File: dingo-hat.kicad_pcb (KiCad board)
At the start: 4 copper layers, 65 x 56.5 mm, 91 parts, among them J1 LiPo-Power, J10 PJ-037B, J11 Bypass-Power, J12 Chassis-Out, J13 i2c_display, J14 WS2812, J15 MPU-9250, J2 Raspberry_Pi_2_3, J201 Bootstrap, J24 3mm_Mount, J25 3mm_Mount, J26 3mm_Mount, J27 3mm_Mount, J3 ULTRA_0, J4 ULTRA_1, J5 LiPo-Balance, J6 0, J7 1, J8 2, J9 3, U1 MCP3021, U2 PCA9685PW, U201 AP9211, U202 MCP73213T-A6BI_MF, U203 BQ29209DRBR, U301 AOZ6605PI-1

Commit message: Updated footprints
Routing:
- net +5V: track 4.96 -> 176.7 mm, vias 16 -> 5
- net +3V3: track 106.7 -> 93.5 mm
- net Net-(F1-Pad2): track 5.06 -> 0.00 mm
- net /SCL_3.3: track 64.5 -> 63.2 mm
- net Net-(J8-Pad3): track 24.9 -> 24.4 mm
- net /SDA_3.3: vias 2 -> 3
- removed copper zone on In2.Cu, net +5V
- removed copper zone on In1.Cu, net GND

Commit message: Changed and re-routed to be 2 layer
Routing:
- net GND: track 46.8 -> 57.2 mm, vias 72 -> 89
- net Net-(FB1-Pad2): track 1.53 -> 6.48 mm
- net Net-(F1-Pad2): track 0.00 -> 4.23 mm
- net /VC0: track 35.0 -> 34.3 mm
- net +5V: track 176.7 -> 176.0 mm
- net /SDA_3.3: track 68.5 -> 69.1 mm, vias 3 -> 2
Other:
- copper layers 4 -> 2

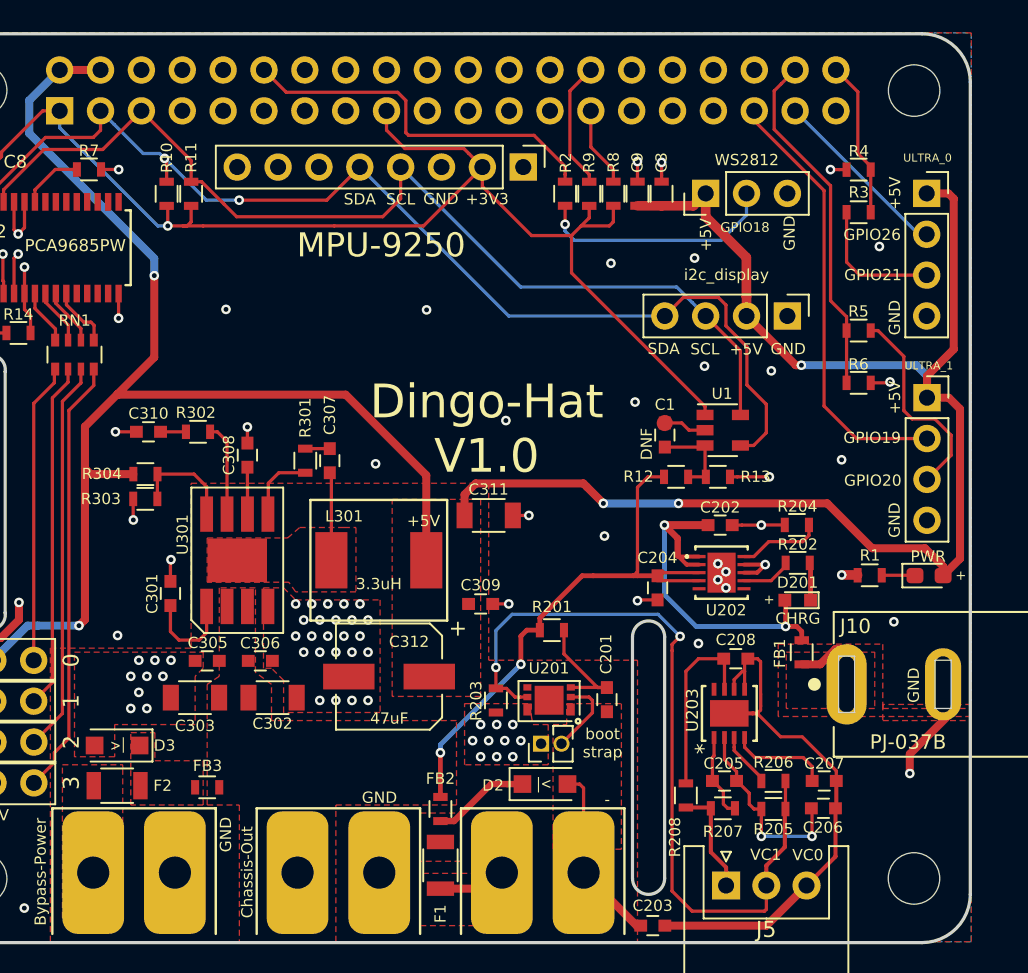
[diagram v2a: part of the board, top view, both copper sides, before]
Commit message: updated footprints to handsolder
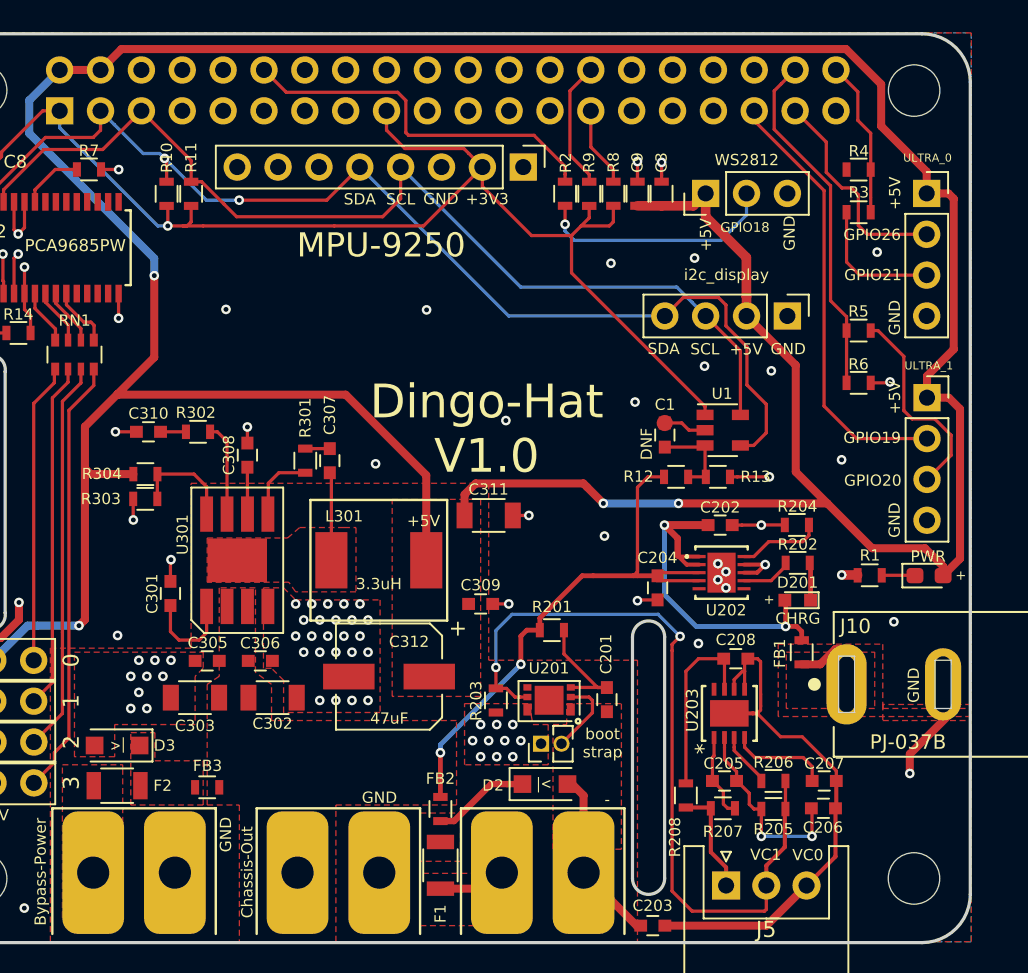
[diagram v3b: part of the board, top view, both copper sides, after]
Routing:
- net +5V: track 176.0 -> 233.6 mm, vias 5 -> 4
- net /GPIO26: track 11.4 -> 13.6 mm
- net GND: track 57.2 -> 56.2 mm, vias 89 -> 88
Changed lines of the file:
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@@
     (thickness 1.6)
     (drawings 94)
-    (tracks 613)
+    (tracks 619)
     (zones 0)
     (modules 91)
@@
   )
   (setup
-    (last_trace_width 0.5)
+    (last_trace_width 0.2032)
     (user_trace_width 0.1524)
     (user_trace_width 0.2032)
@@
   (via (at 144.31 51.444) (size 0.6) (drill 0.3) (layers F.Cu B.Cu) (net 1))
   (segment (start 144.31 52.2408) (end 144.31 51.444) (width 0.2032) (layer F.Cu) (net 1))
-  (segment (start 157.31 51.944) (end 156.8568 51.944) (width 0.2032) (layer F.Cu) (net 1))
-  (via (at 156.31 51.944) (size 0.6) (drill 0.3) (layers F.Cu B.Cu) (net 1))
-  (segment (start 156.8568 51.944) (end 156.31 51.944) (width 0.2032) (layer F.Cu) (net 1))
   (segment (start 148.51 68.144) (end 147.51 68.144) (width 0.2032) (layer F.Cu) (net 1))
   (segment (start 147.06 67.694) (end 146.01 67.694) (width 0.2032) (layer F.Cu) (net 1))
@@
   (via (at 160.25 80.054) (size 0.6) (drill 0.3) (layers F.Cu B.Cu) (net 1))
   (via (at 157 69.984) (size 0.6) (drill 0.3) (layers F.Cu B.Cu) (net 1))
-  (via (at 159.35 56.724) (size 0.6) (drill 0.3) (layers F.Cu B.Cu) (net 1))
+  (via (at 159.21 57.074) (size 0.6) (drill 0.3) (layers F.Cu B.Cu) (net 1))
   (via (at 128.03 70.234) (size 0.6) (drill 0.3) (layers F.Cu B.Cu) (net 1))
   (via (at 148.48 64.164) (size 0.6) (drill 0.3) (layers F.Cu B.Cu) (net 1))
@@
   (segment (start 164.361609 76.133391) (end 164.361609 66.825609) (width 0.5) (layer F.Cu) (net 2))
   (segment (start 163.311 77.184) (end 164.361609 76.133391) (width 0.5) (layer F.Cu) (net 2))
-  (via (at 154.5 64.104) (size 0.6) (drill 0.3) (layers F.Cu B.Cu) (net 2))
   (segment (start 151.09 61.044) (end 154.15 64.104) (width 0.5) (layer F.Cu) (net 2))
-  (segment (start 154.15 64.104) (end 154.5 64.104) (width 0.5) (layer F.Cu) (net 2))
-  (segment (start 162.31 64.774) (end 162.31 66.124) (width 0.5) (layer B.Cu) (net 2))
-  (segment (start 161.64 64.104) (end 162.31 64.774) (width 0.5) (layer B.Cu) (net 2))
-  (segment (start 154.5 64.104) (end 161.64 64.104) (width 0.5) (layer B.Cu) (net 2))
   (segment (start 110.93 45.75) (end 108.39 45.75) (width 0.5) (layer F.Cu) (net 2))
   (segment (start 104.245 82.46) (end 104.235 82.45) (width 0.5) (layer B.Cu) (net 2))
@@
   (segment (start 109.96 67.924) (end 109.96 70.514) (width 0.5) (layer F.Cu) (net 2))
   (segment (start 109.96 70.514) (end 109.96 79.924) (width 0.5) (layer F.Cu) (net 2))
+  (segment (start 162.29 52.074) (end 162.29 53.424) (width 0.5) (layer F.Cu) (net 2))
+  (segment (start 159.459999 49.243999) (end 162.29 52.074) (width 0.5) (layer F.Cu) (net 2))
+  (segment (start 159.459999 46.635997) (end 159.459999 49.243999) (width 0.5) (layer F.Cu) (net 2))
+  (segment (start 157.274001 44.449999) (end 159.459999 46.635997) (width 0.5) (layer F.Cu) (net 2))
+  (segment (start 112.230001 44.449999) (end 157.274001 44.449999) (width 0.5) (layer F.Cu) (net 2))
+  (segment (start 110.93 45.75) (end 112.230001 44.449999) (width 0.5) (layer F.Cu) (net 2))
+  (segment (start 154.15 70.734) (end 156.11 72.694) (width 0.5) (layer F.Cu) (net 2))
+  (segment (start 154.15 64.104) (end 154.15 70.734) (width 0.5) (layer F.Cu) (net 2))
   (segment (start 105.078 62.1) (end 103.478 62.1) (width 0.2032) (layer F.Cu) (net 3))
   (segment (start 103.603 61.975) (end 103.478 62.1) (width 0.2032) (layer F.Cu) (net 3))
@@
   (segment (start 151.57 48.29) (end 151.57 48.904) (width 0.2032) (layer F.Cu) (net 46))
   (segment (start 151.57 48.904) (end 155.91 53.244) (width 0.2032) (layer F.Cu) (net 46))
-  (segment (start 161.784 55.964) (end 162.29 55.964) (width 0.2032) (layer B.Cu) (net 48))
-  (segment (start 154.11 48.29) (end 161.784 55.964) (width 0.2032) (layer B.Cu) (net 48))
+  (segment (start 158.59 55.964) (end 162.29 55.964) (width 0.2032) (layer F.Cu) (net 48))
+  (segment (start 156.047 50.227) (end 156.047 52.110776) (width 0.2032) (layer F.Cu) (net 48))
+  (segment (start 158.04 55.414) (end 158.59 55.964) (width 0.2032) (layer F.Cu) (net 48))
+  (segment (start 154.11 48.29) (end 156.047 50.227) (width 0.2032) (layer F.Cu) (net 48))
+  (segment (start 156.047 52.110776) (end 157.020112 53.083888) (width 0.2032) (layer F.Cu) (net 48))
+  (segment (start 157.020112 53.083888) (end 157.619888 53.083888) (width 0.2032) (layer F.Cu) (net 48))
+  (segment (start 157.619888 53.083888) (end 158.04 53.504) (width 0.2032) (layer F.Cu) (net 48))
+  (segment (start 158.04 53.504) (end 158.04 55.414) (width 0.2032) (layer F.Cu) (net 48))
   (segment (start 157.31 64.5468) (end 157.31 61.95) (width 0.2032) (layer F.Cu) (net 49))
   (segment (start 157.31 65.2) (end 157.31 64.5468) (width 0.2032) (layer F.Cu) (net 49))
@@
   (segment (start 152.81 49.444) (end 152.81 47.05) (width 0.2032) (layer F.Cu) (net 49))
   (segment (start 152.81 47.05) (end 153.260001 46.599999) (width 0.2032) (layer F.Cu) (net 49))
-  (segment (start 158.01 47.11) (end 156.65 45.75) (width 0.2032) (layer F.Cu) (net 50))
-  (segment (start 158.01 50.944) (end 158.01 47.11) (width 0.2032) (layer F.Cu) (net 50))
-  (segment (start 158.81 51.944) (end 158.81 51.744) (width 0.2032) (layer F.Cu) (net 50))
-  (segment (start 158.81 51.744) (end 158.01 50.944) (width 0.2032) (layer F.Cu) (net 50))
   (segment (start 158.81 51.944) (end 158.81 53.694) (width 0.2032) (layer F.Cu) (net 50))
   (segment (start 158.81 53.694) (end 158.81 54.594) (width 0.2) (layer F.Cu) (net 50))
+  (segment (start 158.01 47.11) (end 156.65 45.75) (width 0.2032) (layer F.Cu) (net 50))
+  (segment (start 158.01 48.884) (end 158.01 47.11) (width 0.2032) (layer F.Cu) (net 50))
+  (segment (start 158.81 49.684) (end 158.01 48.884) (width 0.2032) (layer F.Cu) (net 50))
+  (segment (start 158.81 51.944) (end 158.81 49.684) (width 0.2032) (layer F.Cu) (net 50))
   (segment (start 108.11 64.494) (end 108.06 64.544) (width 0.2032) (layer F.Cu) (net 56))
   (segment (start 108.11 64.344) (end 108.11 64.494) (width 0.2032) (layer F.Cu) (net 56))
@@
   (segment (start 141.51 85.71) (end 139.586 87.634) (width 0.2032) (layer F.Cu) (net 66))
   (segment (start 141.51 84.944) (end 141.51 85.71) (width 0.2032) (layer F.Cu) (net 66))
-  (segment (start 140.7132 90.144) (end 139.96 90.144) (width 0.2032) (layer F.Cu) (net 66))
-  (segment (start 140.96 90.3908) (end 140.7132 90.144) (width 0.2032) (layer F.Cu) (net 66))
-  (segment (start 140.96 95.65) (end 140.96 90.3908) (width 0.2032) (layer F.Cu) (net 66))
   (segment (start 144.254 98.944) (end 140.96 95.65) (width 0.5) (layer F.Cu) (net 66))
   (segment (start 144.51 98.944) (end 144.254 98.944) (width 0.5) (layer F.Cu) (net 66))
+  (segment (start 140.25 90.144) (end 140.96 90.854) (width 0.5) (layer F.Cu) (net 66))
+  (segment (start 139.96 90.144) (end 140.25 90.144) (width 0.5) (layer F.Cu) (net 66))
+  (segment (start 140.96 90.854) (end 140.96 95.65) (width 0.5) (layer F.Cu) (net 66))
   (segment (start 142.4 84.134) (end 142.41 84.144) (width 0.2032) (layer F.Cu) (net 67))
   (segment (start 140.166 84.134) (end 142.4 84.134) (width 0.2032) (layer F.Cu) (net 67))

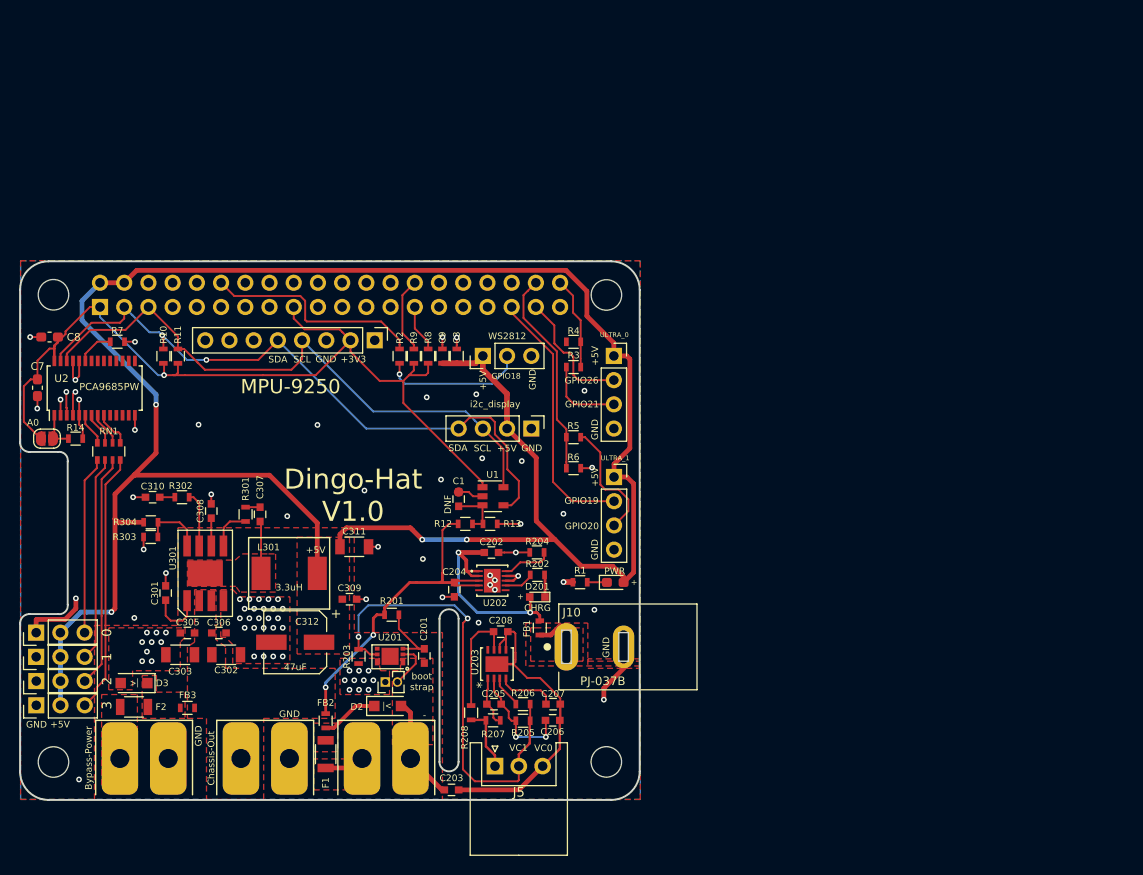
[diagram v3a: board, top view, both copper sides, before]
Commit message: Included both oled and MPU on top.  Additional silkscreen designs
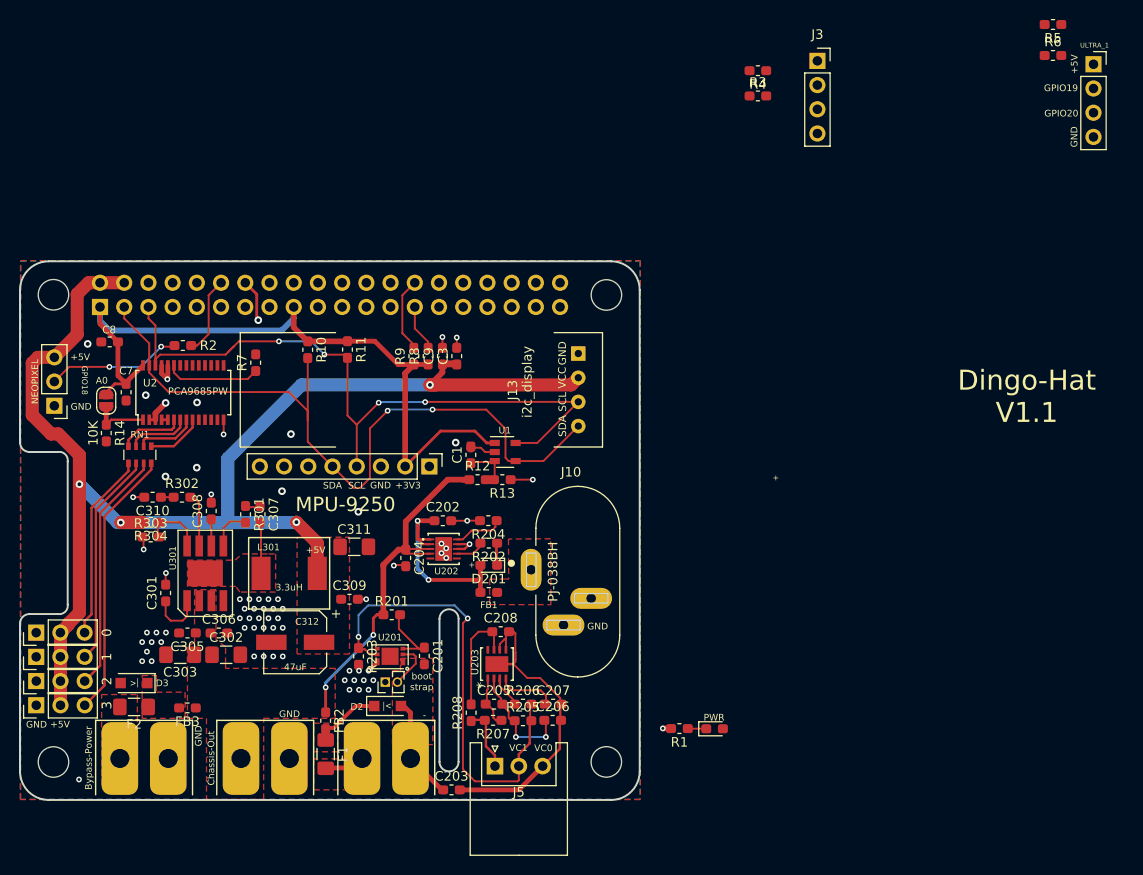
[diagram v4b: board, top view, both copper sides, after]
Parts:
- added G4: LCA2020Logo.3, libs:logo-2020.silk, B.Cu at (266.6, 81.9)
- added G5: LCA2020Logo.4, libs:logo-2020.mask, B.Cu at (266.5, 81.9)
- C1, C201, C202, C203, C204, C205, C206, C207, C208, C301, C305, C306, C307, C308, C309, C310: footprint Capacitors_SMD:C_0603 -> Capacitor_SMD:C_0603_1608Metric_Pad1.05x0.95mm_HandSolder
- C3, C9, FB1, FB2, FB3, R1, R10, R11, R12, R13, R14, R2, R201, R202, R203, R204, R205, R206, R207, R208, R3, R301, R302, R303, R304, R4, R5, R6, R7, R8, R9: footprint Resistors_SMD:R_0603 -> Resistor_SMD:R_0603_1608Metric_Pad1.05x0.95mm_HandSolder
- C302, C303, C311: footprint Capacitors_SMD:C_1206 -> Capacitor_SMD:C_1206_3216Metric_Pad1.42x1.75mm_HandSolder
- D201: footprint LEDs:LED_0603 -> LED_SMD:LED_0603_1608Metric_Pad1.05x0.95mm_HandSolder
- F1, F2: footprint Resistors_SMD:R_1206 -> Resistor_SMD:R_1206_3216Metric_Pad1.42x1.75mm_HandSolder
- J10: value PJ-037B -> PJ-038BH; footprint libs:CUI_PJ-037B -> libs:CUI_PJ-038BH
- J13: footprint Pin_Headers:Pin_Header_Straight_1x04_Pitch2.54mm -> libs:0.91 OLED
- J14: value WS2812 -> NEOPIXEL
- moved G1 100.6 mm to (209.4, 68.8)
- moved G2 80.4 mm to (207.0, 49.4)
- moved G3 80.4 mm to (207.0, 49.4)
- moved R5 66.4 mm to (208.3, 18.7)
- moved R6 66.4 mm to (208.3, 21.9)
- moved J4 66.4 mm to (212.6, 22.8)
- moved J14 45.3 mm to (103.6, 58.7), turned to 180 degrees
- moved J3 37.6 mm to (183.6, 22.5)
- moved R3 34.4 mm to (177.4, 26.2)
- moved R4 34.4 mm to (177.4, 23.5)
- moved R2 22.8 mm to (117.1, 52.3), turned to 180 degrees
- moved D1 18.6 mm to (172.9, 92.5)
- moved R1 18.6 mm to (169.2, 92.5)
- moved R11 17.8 mm to (134.3, 52.8), turned to 270 degrees
- moved R10 15.2 mm to (130.2, 52.8), turned to 270 degrees
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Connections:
- J14 pad 1: +5V -> GND
- J14 pad 3: GND -> +5V
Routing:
- net +5V: track 233.6 -> 141.2 mm
- net /GPIO19: track 27.4 -> 0.00 mm
- net /GPIO20: track 21.9 -> 0.00 mm
- net GND: track 56.2 -> 36.0 mm, vias 88 -> 73
- net /GPIO18: track 23.3 -> 8.25 mm
- net +3V3: track 93.5 -> 78.7 mm, vias 1 -> 0
- net /GPIO26: track 13.6 -> 0.00 mm
- net Net-(J4-Pad3): track 13.0 -> 0.00 mm
- net /SCL_3.3: track 63.2 -> 74.0 mm, vias 0 -> 4
- net /GPIO21: track 9.74 -> 0.00 mm
- net /SDA_3.3: track 69.1 -> 78.4 mm
- net Net-(J3-Pad3): track 8.42 -> 0.00 mm
- net Net-(FB1-Pad2): track 6.48 -> 0.00 mm
- net Net-(R7-Pad1): track 3.89 -> 9.95 mm
- net /PWM0: track 3.43 -> 6.79 mm
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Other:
- board text added: "Dingo-Hat V1.1"
- board text removed: "Dingo-Hat V1.0"
- board text removed: "GPIO21"
- board text removed: "GPIO26"

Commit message: Updated silkscreen. Added button
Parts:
- added SW1: GPIO13, Button_Switch_THT:SW_PUSH_6mm, F.Cu at (156.2, 54.0)
- D2: value 30V 1A -> 30V
- J3, J4: footprint Connector_PinSocket_2.54mm:PinSocket_1x04_P2.54mm_Vertical -> Connector_PinHeader_2.54mm:PinHeader_1x04_P2.54mm_Vertical
- RN1: value 220_Pack04 -> 220x4
- U202: value MCP73213T-A6BI_MF -> MCP73213T
- moved D1 29.7 mm to (161.6, 65.1)
- moved R1 29.7 mm to (157.9, 65.0)
- moved J13 7.15 mm to (135.0, 56.4)
- moved C207 3.17 mm to (159.1, 89.5)
- moved C206 3.17 mm to (159.0, 91.2)
- moved R205 2.49 mm to (155.2, 91.1)
- moved R206 2.49 mm to (155.2, 89.4)
- moved C205 1.69 mm to (151.4, 89.8)
- moved R207 1.69 mm to (151.3, 91.5)
- moved R13 1.62 mm to (151.0, 68.0)
- moved R12 1.61 mm to (147.6, 68.0)
- moved C1 1.57 mm to (147.5, 65.4)
- moved U1 1.57 mm to (151.1, 65.1)
- moved FB2 1.06 mm to (132.1, 90.6)
- moved C203 1.05 mm to (145.2, 97.9)
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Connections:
- J3 pad 1: +5V -> GND
- J3 pad 2: /GPIO26 -> Net-(J3-Pad2)
- J3 pad 3: Net-(J3-Pad3) -> /GPIO26
- J3 pad 4: GND -> +5V
- J4 pad 1: +5V -> GND
- J4 pad 2: /GPIO19 -> Net-(J4-Pad2)
- J4 pad 3: Net-(J4-Pad3) -> /GPIO19
- J4 pad 4: GND -> +5V
- R3 pad 1: Net-(J3-Pad3) -> Net-(J3-Pad2)
- R5 pad 1: Net-(J4-Pad3) -> Net-(J4-Pad2)
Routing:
- net /SDA_3.3: track 78.4 -> 64.5 mm
- net /GPIO13: track 0.00 -> 11.6 mm
- net /SCL_3.3: track 74.0 -> 66.1 mm
- net /VC0: track 34.3 -> 41.8 mm
- net +5V: track 141.2 -> 146.5 mm
- net /VC2: track 6.76 -> 9.97 mm
- net Net-(C207-Pad1): track 6.20 -> 9.06 mm
- net Net-(F1-Pad2): track 4.23 -> 1.41 mm
- net /BatterySupply: track 38.4 -> 36.2 mm
- net Net-(C205-Pad1): track 5.30 -> 3.13 mm
- net Net-(R206-Pad1): track 3.40 -> 5.36 mm
- net Net-(C205-Pad2): track 12.4 -> 13.6 mm
- net Net-(D2-Pad1): track 6.71 -> 5.66 mm
- net /VC1: track 49.2 -> 50.2 mm
- net GND: vias 73 -> 81
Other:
- board size 65 x 56.5 mm -> 65 x 56 mm
- board text added: "1A"
